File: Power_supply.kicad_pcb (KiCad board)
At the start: 2 copper layers, 190 x 110 mm, 16 parts, among them J3 Conn_01x04, J5 220V, J7 Conn_01x04, SW1 SW_Push, U3 6H2P, U4 6H2P

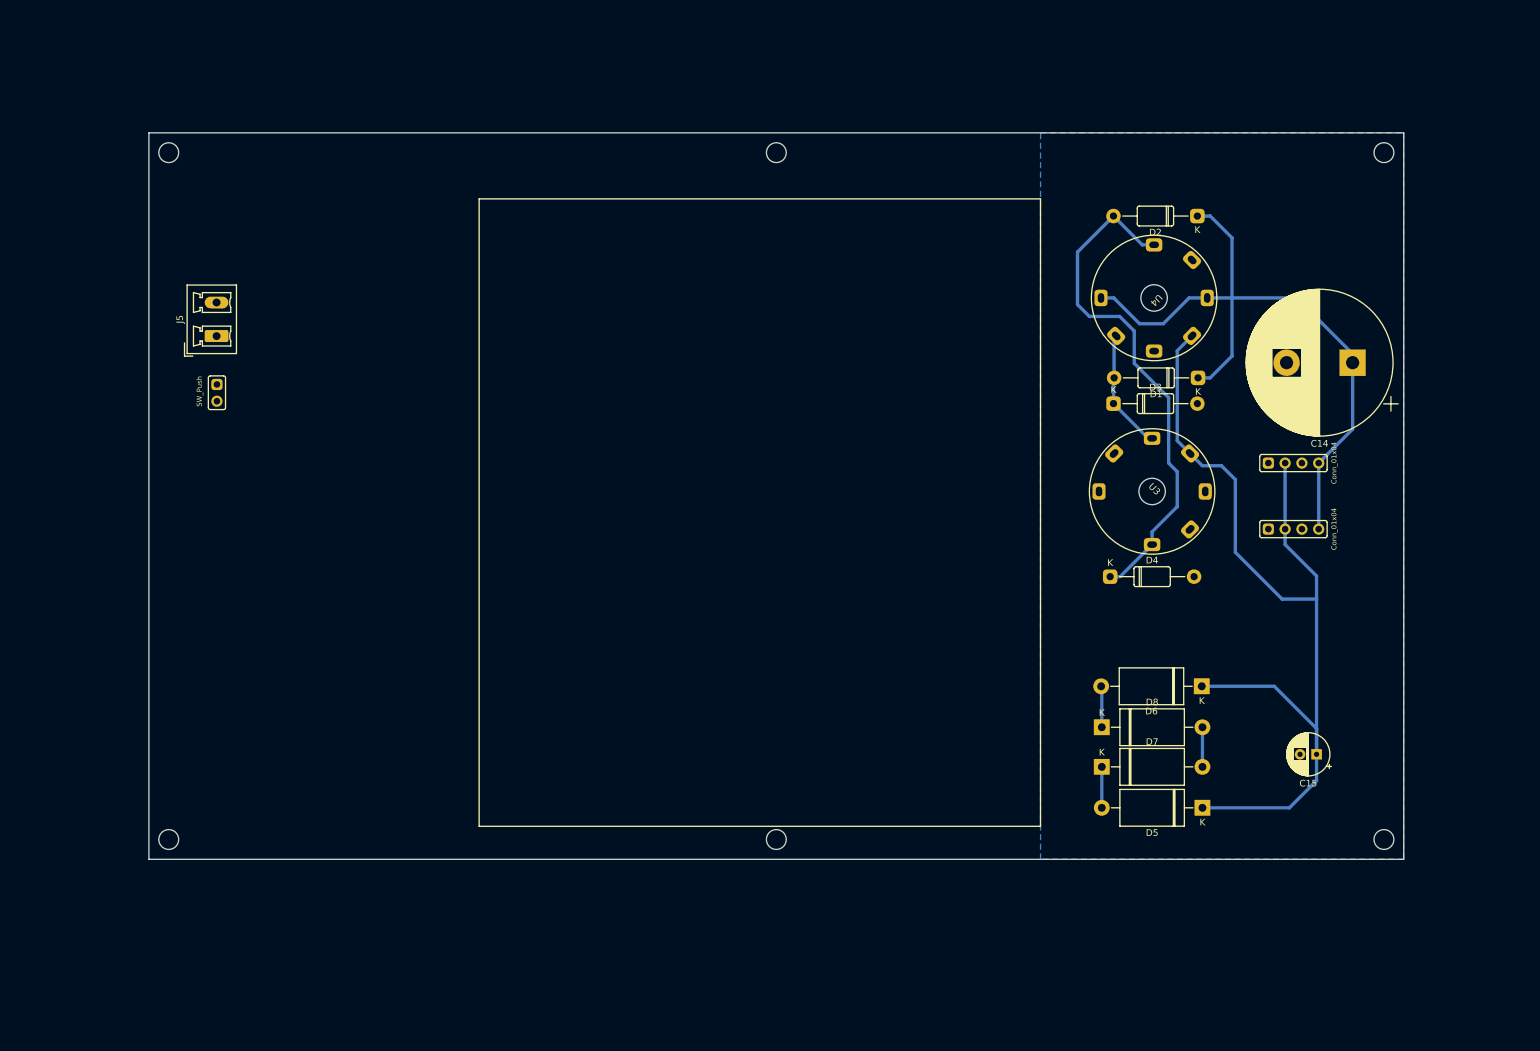
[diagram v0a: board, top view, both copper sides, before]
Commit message: Indication board completed
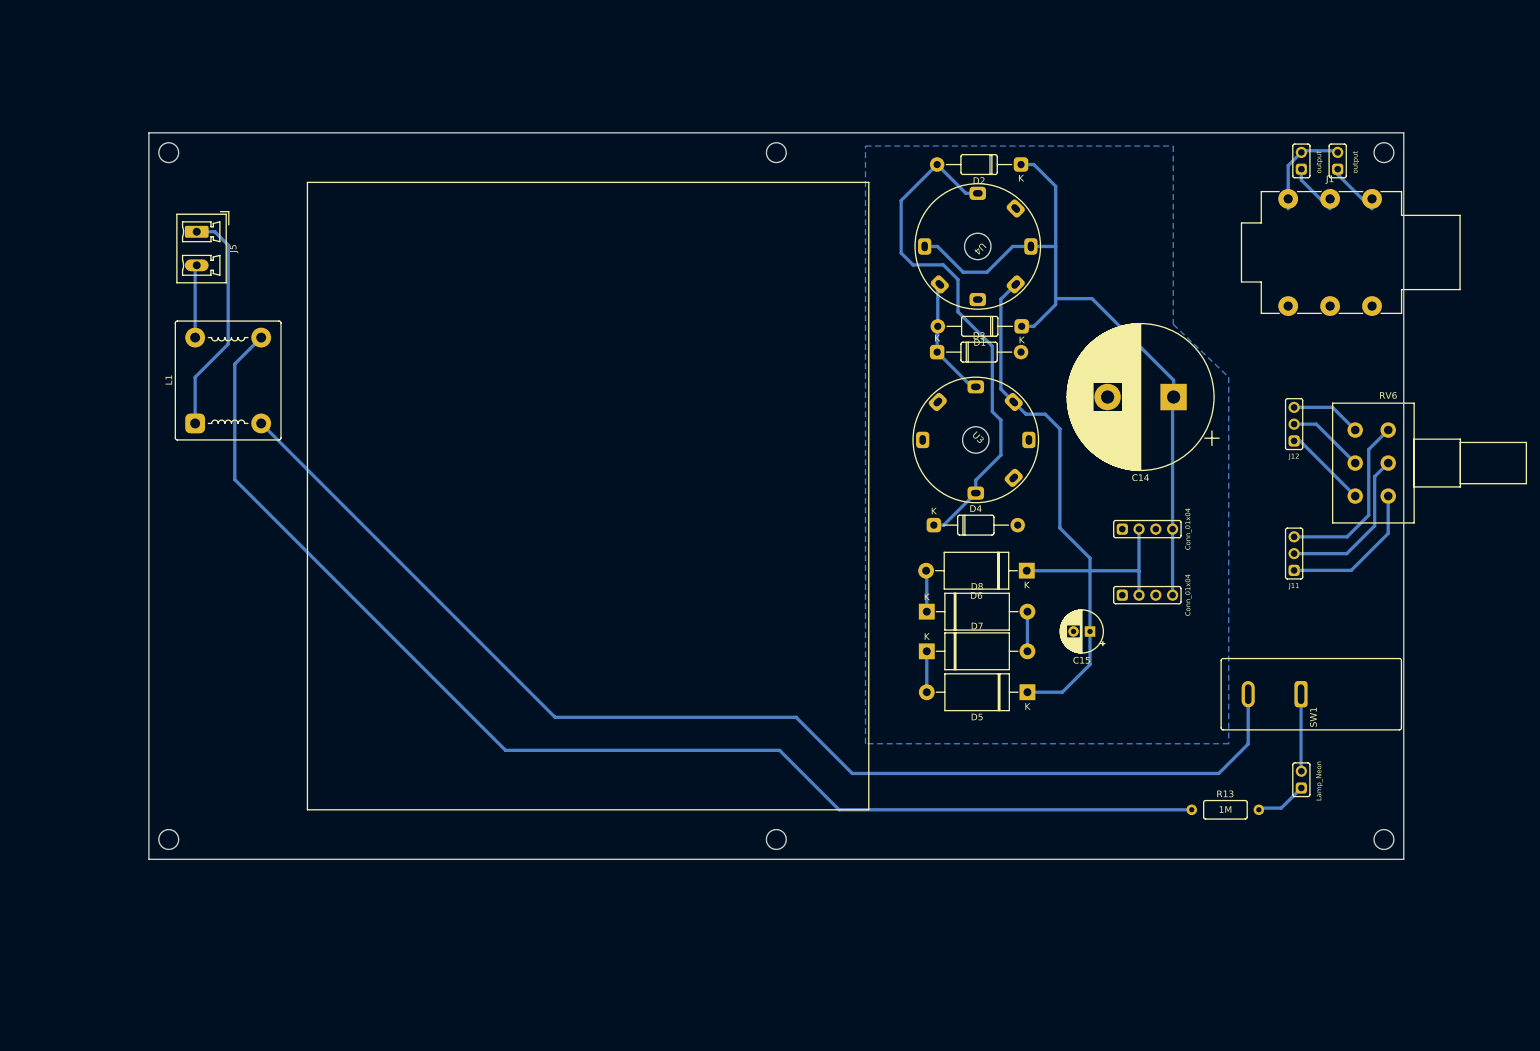
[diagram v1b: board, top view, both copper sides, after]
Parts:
- added J1: AudioJack3, Connector_Audio:Jack_6.35mm_Neutrik_NMJ6HHD2_Horizontal, F.Cu at (222.5, 30.0)
- added J10: output, spdf1626_lib:PinHeader_1x02_P2.54mm, F.Cu at (224.5, 25.5)
- added J11: Conn_01x03, spdf1626_lib:PinHeader_1x03_P2.54mm, F.Cu at (223.4, 86.2)
- added J12: Conn_01x03, spdf1626_lib:PinHeader_1x03_P2.54mm, F.Cu at (223.4, 66.7)
- added J9: output, spdf1626_lib:PinHeader_1x02_P2.54mm, F.Cu at (230.0, 25.5)
- added L1: L_Coupled, spdf1626_lib:L_THT_PLA10, F.Cu at (62.0, 57.5)
- added NE1: Lamp_Neon, spdf1626_lib:PinHeader_1x02_P2.54mm, F.Cu at (224.5, 119.2)
- added R13: 1M, spdf1626_lib:R_THT_025W, F.Cu at (207.9, 122.5)
- added RV6: R_Potentiometer_Dual, Potentiometer_THT:Potentiometer_Alps_RK163_Dual_Horizontal, F.Cu at (237.7, 75.0)
- SW1: footprint spdf1626_lib:PinHeader_1x02_P2.54mm -> Button_Switch_THT:SW_Push_1P2T_Vertical_E-Switch_800UDP8P1A1M6
- moved SW1 170.7 mm to (224.4, 105.0), turned to -90 degrees
- moved C15 39.0 mm to (192.5, 95.5)
- moved D5 31.8 mm to (183.0, 104.7)
- moved D6 31.8 mm to (182.9, 86.3)
- moved D7 31.8 mm to (167.8, 98.5)
- moved D8 31.8 mm to (167.8, 92.5)
- moved D3 27.8 mm to (169.3, 53.2)
- moved D4 27.8 mm to (168.8, 79.4)
- moved U3 27.8 mm to (175.2, 66.5)
- moved D1 27.8 mm to (182.2, 49.3)
- moved D2 27.8 mm to (182.1, 24.8)
- moved U4 27.8 mm to (175.5, 37.2)
- moved C14 27.6 mm to (205.2, 60.0)
- moved J3 24.3 mm to (197.4, 80.0)
- moved J7 24.3 mm to (197.4, 90.0)
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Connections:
- SW1 pad 1: Net-(J5-Pad1) -> Net-(NE1-Pad2)
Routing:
- net Net-(T2-Pad2): track 0.00 -> 188.8 mm
- net Net-(L1-Pad2): track 0.00 -> 181.8 mm
- net +6V: track 147.3 -> 104.1 mm
- net Net-(J5-Pad1): track 0.00 -> 34.7 mm
- net Net-(J11-Pad3): track 0.00 -> 26.8 mm
- net Net-(J11-Pad2): track 0.00 -> 24.3 mm
- net Net-(J11-Pad1): track 0.00 -> 22.2 mm
- net GND: track 6.00 -> 21.1 mm
- net Net-(J12-Pad1): track 0.00 -> 12.7 mm
- net Net-(NE1-Pad2): track 0.00 -> 12.7 mm
- net Net-(J12-Pad2): track 0.00 -> 11.7 mm
- net Net-(J5-Pad2): track 0.00 -> 11.0 mm
- net Net-(J12-Pad3): track 0.00 -> 10.7 mm
- net Net-(J1-PadS): track 0.00 -> 8.15 mm
- net Net-(NE1-Pad1): track 0.00 -> 7.81 mm
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
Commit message: Some cleaning
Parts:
- added J13: Conn_01x04, spdf1626_lib:PinHeader_1x04_P2.54mm, F.Cu at (197.0, 100.0)
- moved J3 0.38 mm to (197.0, 80.0)
- moved J7 0.38 mm to (197.0, 90.0)
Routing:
- net 240V: track 109.7 -> 120.1 mm
- net +6V: track 104.1 -> 113.6 mm
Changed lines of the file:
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@@
     (pad "6" thru_hole circle (at -5 -10) (size 2.34 2.34) (drill 1.3) (layers *.Cu *.Mask)
       (net 21 "Net-(J12-Pad3)") (pinfunction "6") (pintype "passive"))
-    (model "${SPDF1626_3D}/Potentiometer.step"
-      (offset (xyz -6 5 13))
-      (scale (xyz 1 1 1))
-      (rotate (xyz 0 -90 90))
+    (model "${SPDF1626_3D}/Potentiometer_THT_RV16A01F-20.step"
+      (offset (xyz -6.5 5 12.5))
+      (scale (xyz 1 1 1))
+      (rotate (xyz -90 0 -90))
     )
   )
@@
   )
   (footprint "spdf1626_lib:PinHeader_1x04_P2.54mm" (layer "F.Cu")
-    (at 197.38 80 90)
+    (at 197 80 90)
     (descr "Through hole straight pin header, 1x04, 2.54mm pitch, single row")
     (tags "Through hole pin header THT 1x04 2.54mm single row")
@@
       (scale (xyz 1 1 1))
       (rotate (xyz 90 0 180))
+    )
+  )
+  (footprint "spdf1626_lib:PinHeader_1x04_P2.54mm" (layer "F.Cu")
+    (at 197 100 90)
+    (descr "Through hole straight pin header, 1x04, 2.54mm pitch, single row")
+    (tags "Through hole pin header THT 1x04 2.54mm single row")
+    (property "Sheetfile" "Tube_amplifier.kicad_sch")
+    (property "Sheetname" "")
+    (attr through_hole)
+    (fp_text reference "J13" (at 2.64 2.39 90) (layer "F.Fab")
+      (effects (font (size 0.75 0.75) (thickness 0.12)))
+    )
+    (fp_text value "Conn_01x04" (at 0 9.95 90) (layer "F.SilkS")
+      (effects (font (size 0.75 0.75) (thickness 0.12)))
+    )
+    (fp_line (start -1 -1.3) (end 1 -1.3) (layer "F.SilkS") (width 0.12))
+    (fp_line (start -1.3 8.6) (end -1.3 -1) (layer "F.SilkS") (width 0.12))
+    (fp_line (start 1 8.9) (end -1 8.9) (layer "F.SilkS") (width 0.12))
+    (fp_line (start 1.3 -1) (end 1.3 8.6) (layer "F.SilkS") (width 0.12))
+    (fp_arc (start -1 8.9) (mid -1.212132 8.812132) (end -1.3 8.6) (layer "F.SilkS") (width 0.12))
+    (fp_arc (start 1 -1.3) (mid 1.212132 -1.212132) (end 1.3 -1) (layer "F.SilkS") (width 0.12))
+    (fp_arc (start 1.3 8.6) (mid 1.212132 8.812132) (end 1 8.9) (layer "F.SilkS") (width 0.12))
+    (fp_arc (start -1.3 -1) (mid -1.212132 -1.212132) (end -1 -1.3) (layer "F.SilkS") (width 0.12))
+    (pad "1" thru_hole roundrect (at 0 0 90) (size 1.7 1.7) (drill 1) (layers *.Cu *.Mask) (roundrect_rratio 0.25)
+      (net 1 "GND") (pinfunction "Pin_1") (pintype "passive"))
+    (pad "2" thru_hole oval (at 0 2.54 90) (size 1.7 1.7) (drill 1) (layers *.Cu *.Mask)
+      (net 3 "+6V") (pinfunction "Pin_2") (pintype "passive"))
+    (pad "3" thru_hole oval (at 0 5.08 90) (size 1.7 1.7) (drill 1) (layers *.Cu *.Mask)
+      (net 1 "GND") (pinfunction "Pin_3") (pintype "passive"))
+    (pad "4" thru_hole oval (at 0 7.62 90) (size 1.7 1.7) (drill 1) (layers *.Cu *.Mask)
+      (net 2 "240V") (pinfunction "Pin_4") (pintype "passive"))
+    (model "${KISYS3DMOD}/Connector_PinHeader_2.54mm.3dshapes/PinHeader_1x04_P2.54mm_Vertical.wrl"
+      (offset (xyz 0 0 0))
+      (scale (xyz 1 1 1))
+      (rotate (xyz 0 0 0))
     )
   )
@@
   )
   (footprint "spdf1626_lib:PinHeader_1x04_P2.54mm" (layer "F.Cu")
-    (at 197.38 90 90)
+    (at 197 90 90)
     (descr "Through hole straight pin header, 1x04, 2.54mm pitch, single row")
     (tags "Through hole pin header THT 1x04 2.54mm single row")
@@
   (segment (start 224.750001 22.709999) (end 224.5 22.96) (width 0.5) (layer "B.Cu") (net 1))
   (segment (start 187.3 46) (end 187.3 45.1) (width 0.5) (layer "B.Cu") (net 2))
-  (segment (start 205 80) (end 205 60.157832) (width 0.5) (layer "B.Cu") (net 2))
   (segment (start 169.4 37.2) (end 173.3 41.1) (width 0.5) (layer "B.Cu") (net 2))
   (segment (start 184 49.3) (end 187.3 46) (width 0.5) (layer "B.Cu") (net 2))
   (segment (start 173.3 41.1) (end 176.9 41.1) (width 0.5) (layer "B.Cu") (net 2))
-  (segment (start 205 90) (end 205 80) (width 0.5) (layer "B.Cu") (net 2))
   (segment (start 167.45666 37.2) (end 169.4 37.2) (width 0.5) (layer "B.Cu") (net 2))
   (segment (start 176.9 41.1) (end 180.8 37.2) (width 0.5) (layer "B.Cu") (net 2))
@@
   (segment (start 182.15 49.3) (end 184 49.3) (width 0.5) (layer "B.Cu") (net 2))
   (segment (start 205 60.157832) (end 205.157832 60) (width 0.5) (layer "B.Cu") (net 2))
+  (segment (start 204.62 100) (end 204.62 90) (width 0.5) (layer "B.Cu") (net 2))
+  (segment (start 205.157832 60) (end 205.157832 79.462168) (width 0.5) (layer "B.Cu") (net 2))
+  (segment (start 204.62 90) (end 204.62 80) (width 0.5) (layer "B.Cu") (net 2))
+  (segment (start 205.157832 79.462168) (end 204.62 80) (width 0.5) (layer "B.Cu") (net 2))
   (segment (start 187.3 45.1) (end 187.3 37.2) (width 0.5) (layer "B.Cu") (net 2))
   (segment (start 184 24.8) (end 182.05 24.8) (width 0.5) (layer "B.Cu") (net 2))
@@
   (segment (start 205.157832 60) (end 205.157832 57.457832) (width 0.5) (layer "B.Cu") (net 2))
   (segment (start 205.157832 57.457832) (end 192.8 45.1) (width 0.5) (layer "B.Cu") (net 2))
-  (segment (start 199.92 86.42) (end 199.92 90) (width 0.5) (layer "B.Cu") (net 3))
   (segment (start 188.3 104.7) (end 192.5 100.5) (width 0.5) (layer "B.Cu") (net 3))
+  (segment (start 192.5 86.3) (end 199.48 86.3) (width 0.5) (layer "B.Cu") (net 3))
   (segment (start 180.945243 60.754757) (end 182.790486 62.6) (width 0.5) (layer "B.Cu") (net 3))
   (segment (start 192.5 86.3) (end 192.5 95.5) (width 0.5) (layer "B.Cu") (net 3))
@@
   (segment (start 192.5 100.5) (end 192.5 95.5) (width 0.5) (layer "B.Cu") (net 3))
   (segment (start 182.790486 62.6) (end 185.7 62.6) (width 0.5) (layer "B.Cu") (net 3))
-  (segment (start 199.92 80) (end 199.92 86.42) (width 0.5) (layer "B.Cu") (net 3))
   (segment (start 179 45.190486) (end 179 58.809514) (width 0.5) (layer "B.Cu") (net 3))
-  (segment (start 199.8 86.3) (end 199.92 86.42) (width 0.5) (layer "B.Cu") (net 3))
+  (segment (start 199.54 90) (end 199.54 86.36) (width 0.5) (layer "B.Cu") (net 3))
+  (segment (start 199.48 86.3) (end 199.54 86.36) (width 0.5) (layer "B.Cu") (net 3))
   (segment (start 183.02 104.7) (end 188.3 104.7) (width 0.5) (layer "B.Cu") (net 3))
+  (segment (start 199.54 100) (end 199.54 90) (width 0.5) (layer "B.Cu") (net 3))
   (segment (start 179 58.809514) (end 180.945243 60.754757) (width 0.5) (layer "B.Cu") (net 3))
   (segment (start 181.245243 42.945243) (end 179 45.190486) (width 0.5) (layer "B.Cu") (net 3))
-  (segment (start 192.5 86.3) (end 199.8 86.3) (width 0.5) (layer "B.Cu") (net 3))
+  (segment (start 199.54 86.36) (end 199.54 80) (width 0.5) (layer "B.Cu") (net 3))
   (segment (start 192.5 84.4) (end 192.5 86.3) (width 0.5) (layer "B.Cu") (net 3))
   (segment (start 187.94 79.84) (end 192.5 84.4) (width 0.5) (layer "B.Cu") (net 3))
